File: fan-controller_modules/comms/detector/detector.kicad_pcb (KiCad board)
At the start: 4 copper layers, 88.9 x 50.8 mm, 46 parts, among them J101 CONN_01X03, J102 CONN_01X02, J103 CONN_01X02, Q101 BC556, Q102 BC556, Q103 BC546, Q104 BC546, Q105 BC546, Q106 BC546, Q107 BC546, Q108 BC546, U101 TL061, U102 TL061, U103 TL061

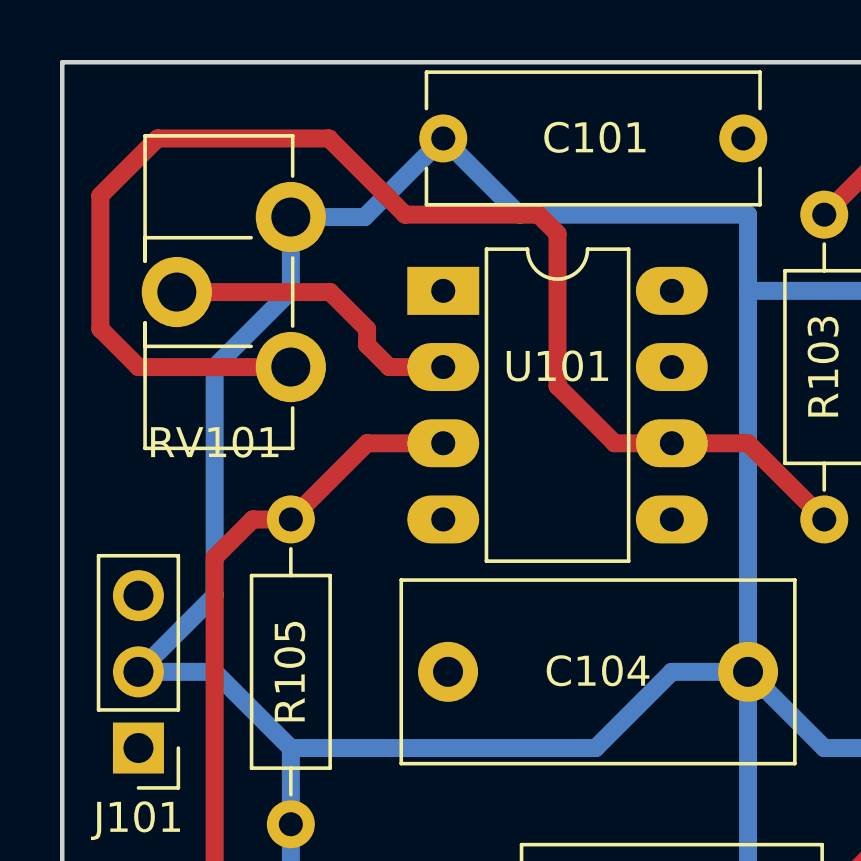
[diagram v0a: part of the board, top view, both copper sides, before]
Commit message: Comms: Detector module
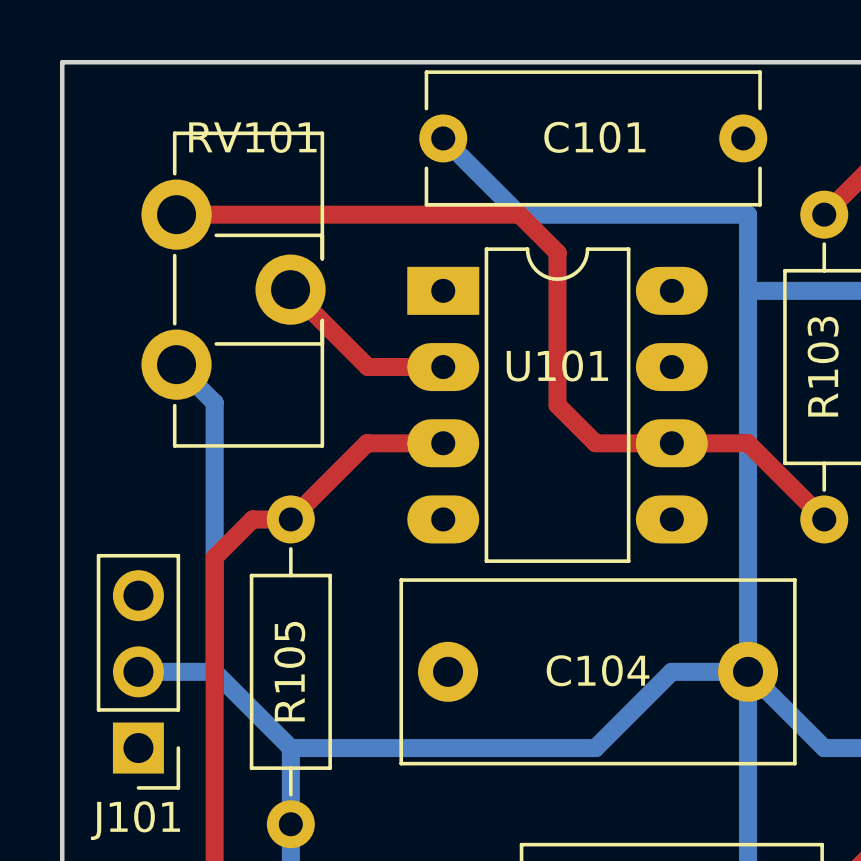
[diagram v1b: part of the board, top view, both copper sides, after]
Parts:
- moved RV101 6.35 mm to (100.3, 81.3), turned to 0 degrees
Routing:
- net /_VCC: track 241.9 -> 219.9 mm
- net Net-(R103-Pad1): track 44.5 -> 28.8 mm
- net GND: track 542.9 -> 530.2 mm
- net Net-(RV101-Pad2): track 10.2 -> 6.16 mm
